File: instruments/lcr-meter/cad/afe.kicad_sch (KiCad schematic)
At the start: 28 parts, among them J3 DUT HI / LO, U6 OPA2810IDGKR, U7 OPA2810IDGKR

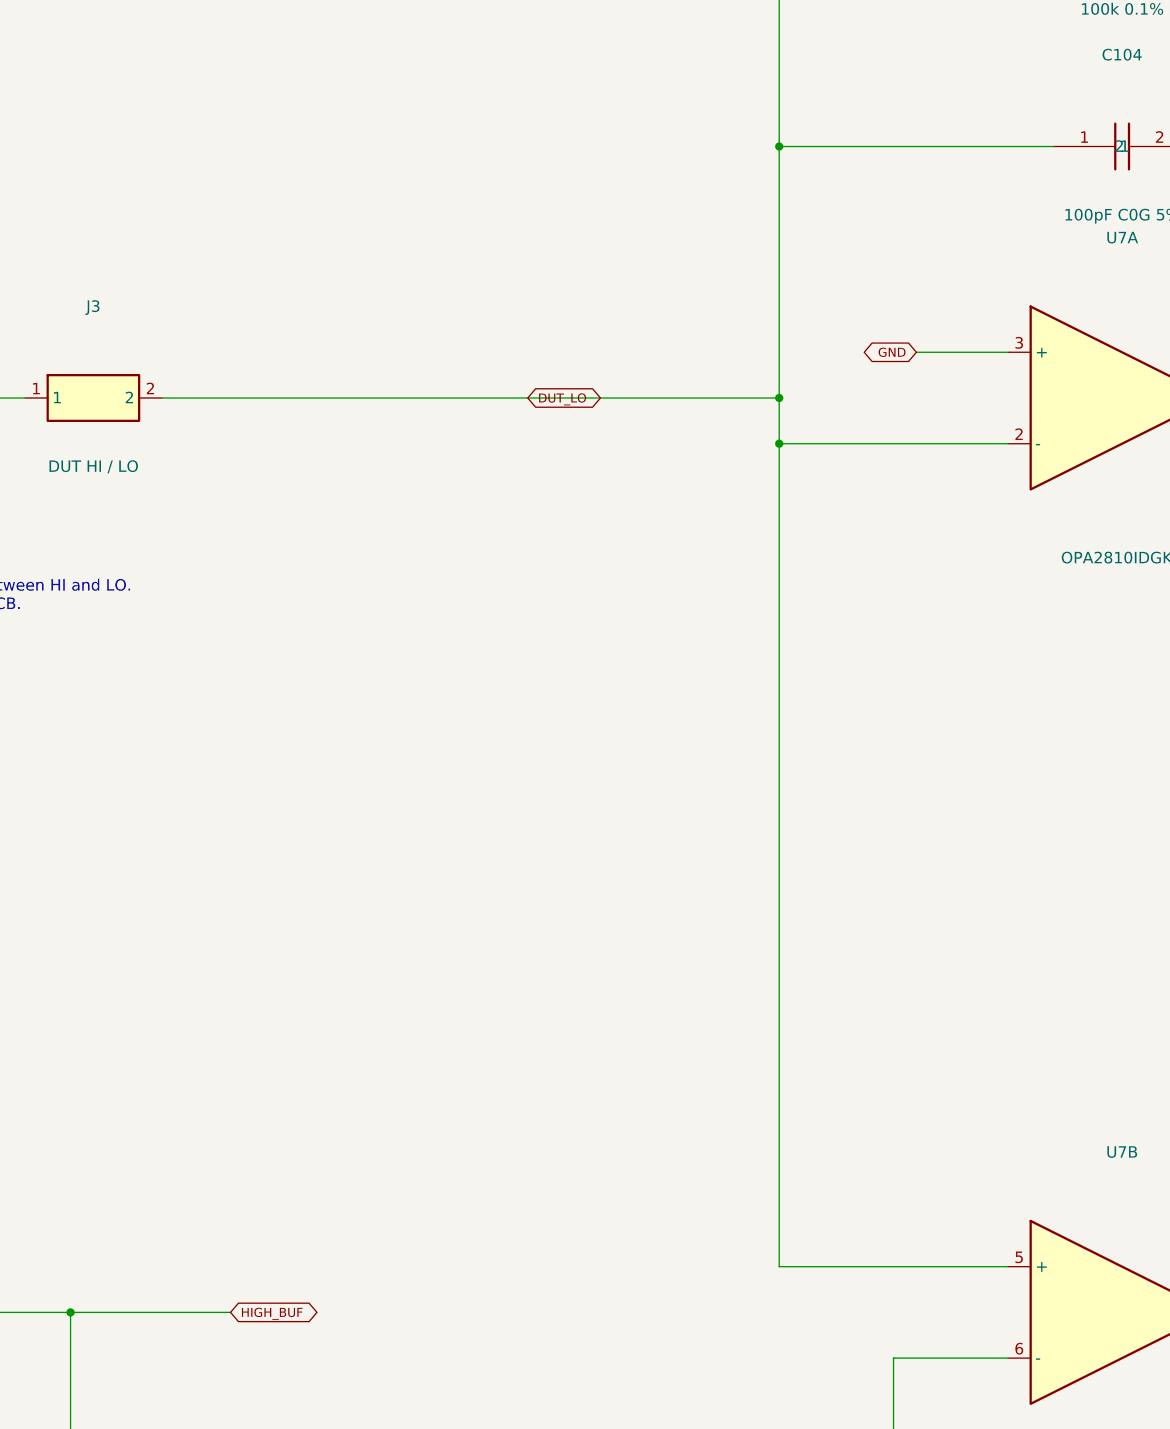
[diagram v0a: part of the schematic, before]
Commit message: lcr-meter Rev D: R94 22 ohm LO isolation, R83 1.74M
- R94 (RT0603BRD0722RL, 22R 0.1% 25ppm) at (167.0,105.3) between J3 LO
  (DUT_LO) and the new TIA_SUM net (U7.2, C104.1, R43-R45.1). The LOW
  follower (U7.5) keeps the J3 F.Cu route, so channel A is the DUT voltage.
  J3.2 reaches R94.1 by a new B.Cu branch and via; the U7 under-body link
  now rises to R94.2; new In1/In2/B keepout under R94.2. Hand-routed per
  validation/layout-parasitics (placement shifted up 0.1 mm for courtyard).
- R83 1.78M -> 1.74M (0603WAF1744T5E) per validation/power-spurs R6.
- AFE schematic page draws R94 with the LOW tap on the J3 side; title
  blocks and silk say Rev D; U7 reference moved clear of R94.
- Adds cad/tools/dump_copper.py + region_view.py for hand-routing views.

rebuild.sh: ERC 0, DRC 0, 0 unconnected, schematic parity 0, DFM audit pass.
LCSC stock for the new lines is to be confirmed at JLC BOM upload.

Co-Authored-By: Claude Opus 5.5 <noreply@anthropic.com>
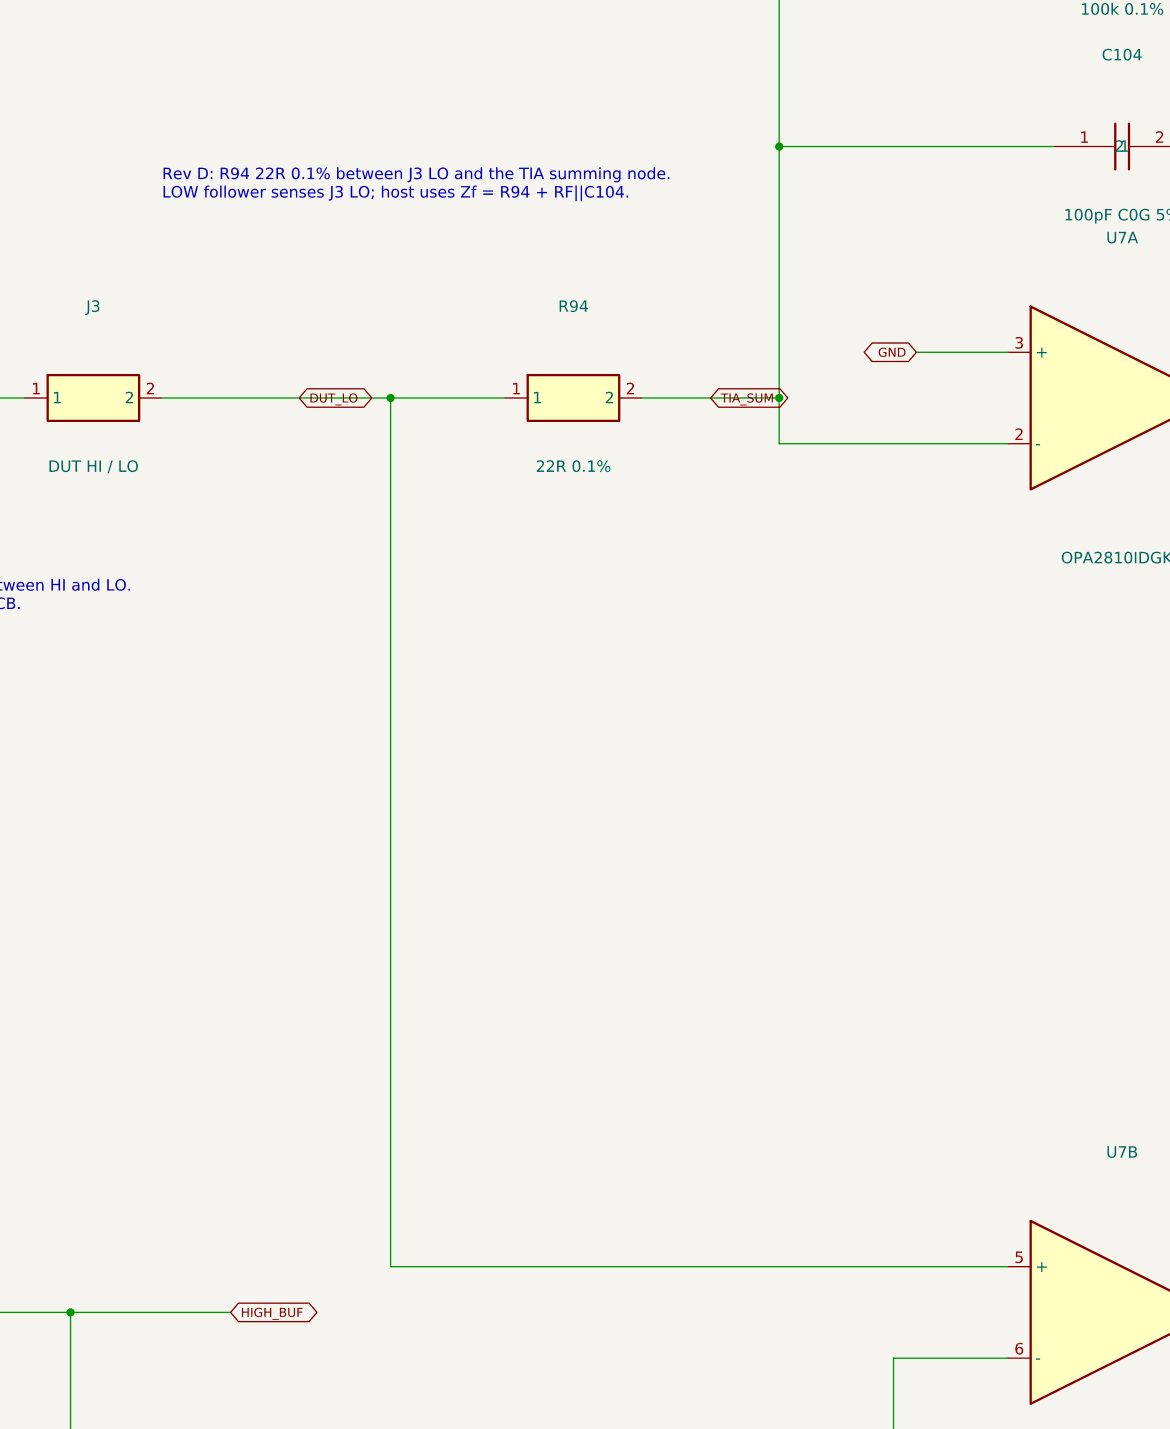
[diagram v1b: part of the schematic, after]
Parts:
- added R94: 22R 0.1%, LCR:R_0603_1608Metric, symbol LCR:AFE_R
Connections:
- net DUT_LO: now also R94.1; no longer C104.1, R43.1, R44.1, R45.1, U7.2 (-)
- new net TIA_SUM: C104.1, R43.1, R44.1, R45.1, R94.2, U7.2 (-)
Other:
- note added: "Rev D: R94 22R 0.1% between J3 LO and the TIA summing node. LOW follower senses J3 LO; host uses Zf = R94 + RF||C104."

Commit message: feat(lcr): Rev E board with TAC5112 codec front end and relay ranges
Hand-routed Rev E on the Rev D outline:
- removes the ADS9224R, AD9833, both THS4551s, FB2 and JP1-JP6;
- adds the TAC5112 with its own AP2112K for 3V3A, three TQ2SA latching
  relays and their AO3400A drivers.

cad/tools/rev_e.py builds design.json and routing.json from the Rev D
package. rev_e_routes.py gives every new segment and via by coordinate.

Details:
- Every via is now a 0.3 mm drill with a pad of 0.45 mm or more.
  The board rules set a 0.30 mm minimum hole and a 0.075 mm minimum
  annular ring.
- Basic-library swaps: D1 is now SRV05-4, and SW1/SW2 are now TS-1088.
- placement_offsets.py adds JLC CPL offsets for the new keyed parts,
  read from the lceda.cn EasyEDA mirror (easyeda.com returns 403). It
  reproduces the audited offsets for U3 (270) and Q1 (180).

Checks:
- rebuild.sh: ERC 0, DRC 0 violations and 0 unconnected, parity 0.
- package_cad and audit_dfm pass: 34 intended via-in-pad, none
  unexpected.
- independent_check.py e: 575 pins, 0 findings.

Co-Authored-By: Claude Opus 5.5 <noreply@anthropic.com>
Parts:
- removed JP1: RG 100R, LCR:PinHeader_1x02_P2.54mm_Vertical, symbol LCR:AFE_JP
- removed JP2: RG 5k, LCR:PinHeader_1x02_P2.54mm_Vertical, symbol LCR:AFE_JP
- removed JP3: RG 100k, LCR:PinHeader_1x02_P2.54mm_Vertical, symbol LCR:AFE_JP
- removed JP4: RF 100R, LCR:PinHeader_1x02_P2.54mm_CompactCourtyard, symbol LCR:AFE_JPR
- removed JP5: RF 5k, LCR:PinHeader_1x02_P2.54mm_Vertical, symbol LCR:AFE_JPR
- removed JP6: RF 100k, LCR:PinHeader_1x02_P2.54mm_Vertical, symbol LCR:AFE_JPR
- added C78: 100pF C0G 5%, LCR:C_0603_1608Metric, symbol LCR:AFE_C
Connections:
- net DUT_LO: now also C78.1
- net GND: now also C78.2
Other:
- note added: "Rev E: C78 100pF C0G from J3 LO to GND (TIA margin with relay parasitics)."
- note added: "U6A source buffer; U6B HI sense; U7A transimpedance; U7B LO sense. Ranges: latching relays K1/K2/K3 (range sheet) close one matched RG/RF pair. One local C104=100pF compensates all ranges; C78 100pF DUT_LO to GND (Rev E stability). No BUF634A: maximum source current approximately 18mA. Isolated, discharged DUT only."
- note removed: "U6A source buffer; U6B HI sense; U7A transimpedance; U7B LO sense. Fit ONE MATCHED pair: JP1+JP4=100R; JP2+JP5=5k; JP3+JP6=100k. Power OFF to change ranges. One local C104=100pF compensates all ranges. No BUF634A: maximum source current approximately 18mA. Isolated, discharged DUT only."

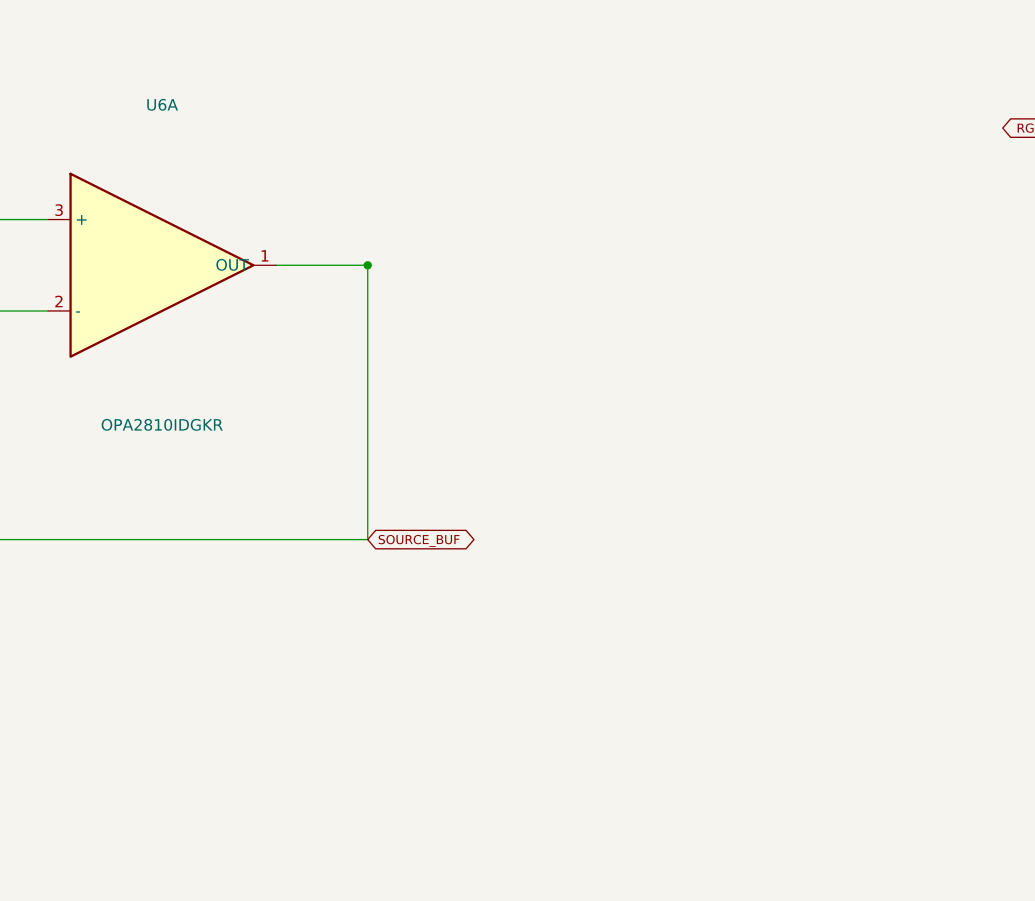
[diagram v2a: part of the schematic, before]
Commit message: fix(lcr): isolate the Rev E source driver from the relay bus
The extracted Rev E layout took the source-driver loop to 38.46 deg at
stress relay values (b1ff84f37). Two changes:

- R104 47 ohm (C23182, basic) sits between U6A and SOURCE_BUF.
  U6A's feedback stays at the pin, and its output is now net SRC_DRV.
- The SOURCE_BUF In2 run moves from x 188.8 to x 185.5, 3.4 mm clear
  of DUT_HI on B.Cu (stacked, the two coupled 2.4 pF).

The harness's _srciso47 case projected 47.3 deg at stress. The board
is being re-extracted to confirm.

Checks:
- rebuild.sh: ERC 0, DRC 0 / 0 unconnected, parity 0; package and DFM
  pass.
- independent_check.py e: 577 pins, 0 findings.

Five boards: $416.59.

Co-Authored-By: Claude Opus 5.5 <noreply@anthropic.com>
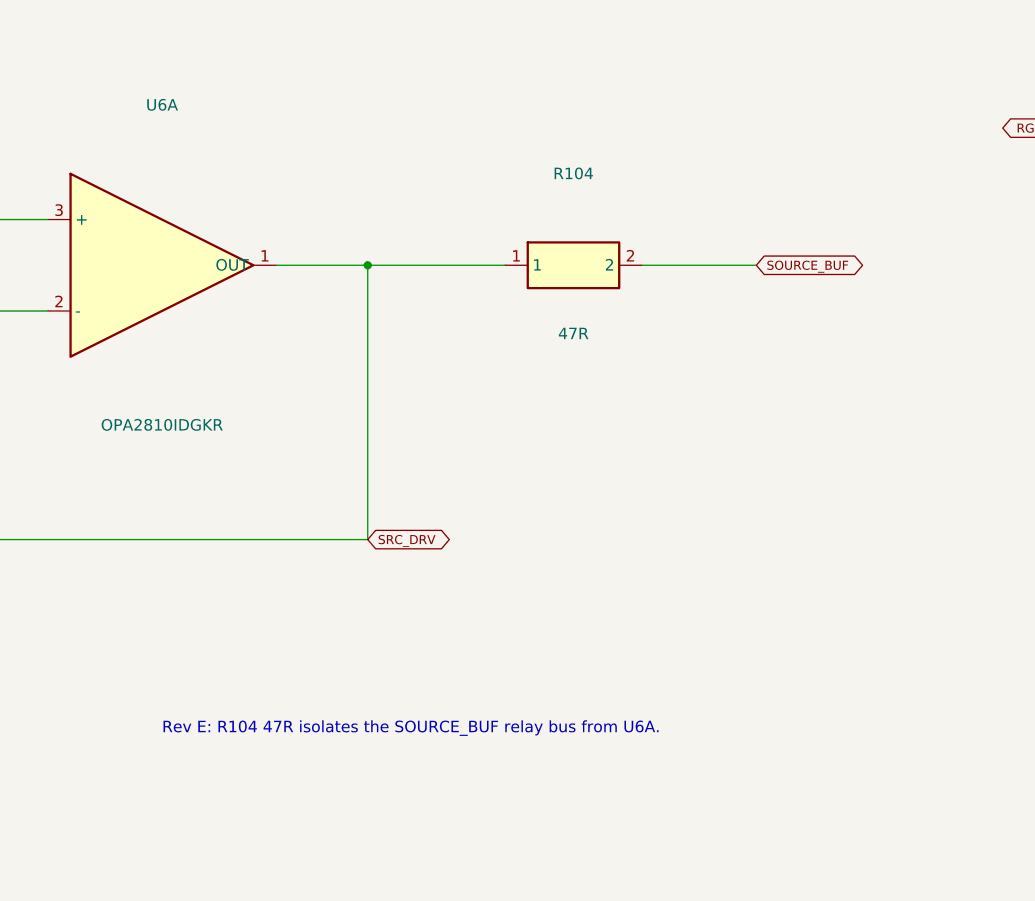
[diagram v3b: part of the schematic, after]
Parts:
- added R104: 47R, LCR:R_0603_1608Metric, symbol LCR:AFE_R
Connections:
- net SOURCE_BUF: now also R104.2; no longer U6.1 (OUT), U6.2 (-)
- new net SRC_DRV: R104.1, U6.1 (OUT), U6.2 (-)
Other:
- note added: "Rev E: R104 47R isolates the SOURCE_BUF relay bus from U6A."

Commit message: Rev E board: four-terminal BNC jacks, K4 reference relay
- J3 header -> four SAMZO BNC-KYWE-295-W4-N (C41416668, hand fit) on the
  top edge at 22 mm pitch: J3 HCUR (DUT_HI), J7 HPOT, J8 LPOT, J9 LCUR
  (DUT_LO). Followers U6.5/U7.5 now sense HPOT/LPOT. R105/R106 1k (basic
  C21190) tie POT to CUR for two-terminal leads. Board 140 x 105 mm.
- K4 TQ2SA: COM2 = HCUR, NO2 -> R107 1k 0.1 % -> LCUR; RESET on the
  shared RLY_RST, SET on Q6/GPIO14 (GPIO12's pad is boxed in by USB_SENSE).
- C78 moves onto the LCUR run. All copper hand-specified in rev_e_routes.py.
- rebuild: ERC 0, DRC 0 / 0 unconnected, parity PASS; independent_check
  620 pins, 0 findings (topology check updated for 4T).
- Five boards $453.46 (+$36.87); 5 PCBs / 2 assembled $309.31.

Co-Authored-By: Claude Opus 5.5 <noreply@anthropic.com>
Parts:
- added J7: BNC HPOT, LCR:BNC_SAMZO_KYWE-295-W4-N_Horizontal, symbol LCR:AFE_BNC
- added J8: BNC LPOT, LCR:BNC_SAMZO_KYWE-295-W4-N_Horizontal, symbol LCR:AFE_BNC
- added J9: BNC LCUR, LCR:BNC_SAMZO_KYWE-295-W4-N_Horizontal, symbol LCR:AFE_BNC
- added R105, R106: 1k, LCR:R_0603_1608Metric, symbol LCR:AFE_R
- J3: value DUT HI / LO -> BNC HCUR; footprint LCR:PinHeader_1x02_P2.54mm_Vertical -> LCR:BNC_SAMZO_KYWE-295-W4-N_Horizontal; symbol LCR:AFE_DUT -> LCR:AFE_BNC; LCSC C7402729 -> C41416668; MPN TSW-102-07-G-S -> BNC-KYWE-295-W4-N; Manufacturer Samtec -> SAMZO; Unit_USD 0.3002 -> 1.29
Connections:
- net DUT_HI: now also J3.5, R105.1; no longer J3.1, U6.5 (+)
- net DUT_LO: now also J9.5, R106.1; no longer J3.2, U7.5 (+)
- net GND: now also J3.1, J3.2, J3.3, J3.4, J7.1, J7.2, J7.3, J7.4, J8.1, J8.2, J8.3, J8.4, J9.1, J9.2, J9.3, J9.4
- new net HPOT: J7.5, R105.2, U6.5 (+)
- new net LPOT: J8.5, R106.2, U7.5 (+)
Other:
- note added: "J3 HCUR, J7 HPOT, J8 LPOT, J9 LCUR: BNC, 22 mm pitch, shells to GND. Connect an external, isolated, discharged DUT with Kelvin leads. R105/R106 1k tie each POT to its CUR for two-terminal leads."
- note added: "Rev D: R94 22R 0.1% between LCUR and the TIA summing node. Rev E: LOW follower senses LPOT; host uses Zf = R94 + RF||C104."
- note added: "Rev E: C78 100pF C0G from LCUR (DUT_LO) to GND (TIA margin with relay parasitics)."
- note added: "U6A source buffer; U6B HI sense; U7A transimpedance; U7B LO sense. Ranges: latching relays K1/K2/K3 (range sheet) close one matched RG/RF pair. Four-terminal BNC jacks: HCUR = DUT_HI, LCUR = DUT_LO; followers sense HPOT / LPOT. One local C104=100pF compensates all ranges; C78 100pF DUT_LO to GND (Rev E stability). No BUF634A: maximum source current approximately 18mA. Isolated, discharged DUT onl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"
- note removed: "J3: connect external, isolated DUT between HI and LO. No DUT component is fitted on this PCB."
- note removed: "Rev D: R94 22R 0.1% between J3 LO and the TIA summing node. LOW follower senses J3 LO; host uses Zf = R94 + RF||C104."
- note removed: "Rev E: C78 100pF C0G from J3 LO to GND (TIA margin with relay parasitics)."
- note removed: "U6A source buffer; U6B HI sense; U7A transimpedance; U7B LO sense. Ranges: latching relays K1/K2/K3 (range sheet) close one matched RG/RF pair. One local C104=100pF compensates all ranges; C78 100pF DUT_LO to GND (Rev E stability). No BUF634A: maximum source current approximately 18mA. Isolated, discharged DUT only."

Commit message: lcr-meter: Rev E cost pass: tented vias (no POFV), two extended lines freed, 2k/5k 0.1 % restocked at 25 ppm
Five vias moved off small SMT lands (R3.2, C44.1, R101.1, U16.2, Y1.4); the 33
exposed-pad thermal vias stay, tented on B.Mask. audit_dfm.py now fails on a via
ring touching a land and on any untented via. Boost divider 430k/40.2k with 15 pF
and 4.7 pF feed-forward (preferred/basic). R32/R33 and R41/R44 move to Viking
25 ppm/C thin film (C728588 down to 22 in stock; the 5k was 50 ppm/C against the
budget). ERC 0, DRC 0/0/0, independent check 0, layout audit unchanged.
Five boards: $458.02 -> $428.40.

Co-Authored-By: Claude Opus 5.5 <noreply@anthropic.com>
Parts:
- R41, R44: LCSC C862232 -> C2828621; MPN RT0603BRE075KL -> AR03BTCX5001; Manufacturer YAGEO -> Viking Tech; Unit_USD 0.0262 -> 0.0318
